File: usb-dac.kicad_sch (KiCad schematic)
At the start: 1 part, among them U1 PCM2706CPJTR

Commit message: Update schematic
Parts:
- removed U1: PCM2706CPJTR, PJT32, symbol 2024-07-12_02-06-17:PCM2706CPJTR
- added P1: USB_C_Plug_USB2.0, symbol Connector:USB_C_Plug_USB2.0
- added U1: PCM2912APJTR, PJT32, symbol 2024-07-12_22-03-46:PCM2912APJTR
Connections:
- new net: P1.A4 (VBUS), P1.A9 (VBUS), P1.B4 (VBUS), P1.B9 (VBUS)
- new net GND: P1.A1 (GND), P1.A12 (GND), P1.B1 (GND), P1.B12 (GND), P1.S1 (SHIELD)
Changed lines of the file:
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@@
 	(paper "A4")
 	(symbol
-		(lib_id "2024-07-12_02-06-17:PCM2706CPJTR")
-		(at 106.68 81.28 0)
+		(lib_id "Connector:USB_C_Plug_USB2.0")
+		(at 67.31 101.6 0)
+		(unit 1)
+		(exclude_from_sim no)
+		(in_bom yes)
+		(on_board yes)
+		(dnp no)
+		(fields_autoplaced yes)
+		(property "Reference" "P1"
+			(at 67.31 78.74 0)
+			(effects
+				(font
+					(size 1.27 1.27)
+				)
+			)
+		)
+		(property "Value" "USB_C_Plug_USB2.0"
+			(at 67.31 81.28 0)
+			(effects
+				(font
+					(size 1.27 1.27)
+				)
+			)
+		)
+		(property "Footprint" ""
+			(at 71.12 101.6 0)
+			(effects
+				(font
+					(size 1.27 1.27)
+				)
+				(hide yes)
+			)
+		)
+		(property "Datasheet" "https://www.usb.org/sites/default/files/documents/usb_type-c.zip"
+			(at 71.12 101.6 0)
+			(effects
+				(font
+					(size 1.27 1.27)
+				)
+				(hide yes)
+			)
+		)
+		(property "Description" "USB 2.0-only Type-C Plug connector"
+			(at 67.31 101.6 0)
+			(effects
+				(font
+					(size 1.27 1.27)
+				)
+				(hide yes)
+			)
+		)
+		(pin "B9"
+		)
+		(pin "S1"
+		)
+		(pin "B12"
+		)
+		(pin "B5"
+		)
+		(pin "B1"
+		)
+		(pin "A5"
+		)
+		(pin "A7"
+		)
+		(pin "A4"
+		)
+		(pin "A1"
+		)
+		(pin "B4"
+		)
+		(pin "A9"
+		)
+		(pin "A12"
+		)
+		(pin "A6"
+		)
+		(instances
+			(project ""
+				(path "/4a7efef3-c114-4eaa-9004-9ebc24c78436"
+					(reference "P1")
+					(unit 1)
+				)
+			)
+		)
+	)
+	(symbol
+		(lib_id "power:GND")
+		(at 67.31 124.46 0)
+		(unit 1)
+		(exclude_from_sim no)
+		(in_bom yes)
+		(on_board yes)
+		(dnp no)
+		(fields_autoplaced yes)
+		(property "Reference" "#PWR01"
+			(at 67.31 130.81 0)
+			(effects
+				(font
+					(size 1.27 1.27)
+				)
+				(hide yes)
+			)
+		)
+		(property "Value" "GND"
+			(at 67.31 129.54 0)
+			(effects
+				(font
+					(size 1.27 1.27)
+				)
+			)
+		)
+		(property "Footprint" ""
+			(at 67.31 124.46 0)
+			(effects
+				(font
+					(size 1.27 1.27)
+				)
+				(hide yes)
+			)
+		)
+		(property "Datasheet" ""
+			(at 67.31 124.46 0)
+			(effects
+				(font
+					(size 1.27 1.27)
+				)
+				(hide yes)
+			)
+		)
+		(property "Description" "Power symbol creates a global label with name \"GND\" , ground"
+			(at 67.31 124.46 0)
+			(effects
+				(font
+					(size 1.27 1.27)
+				)
+				(hide yes)
+			)
+		)
+		(pin "1"
+		)
+		(instances
+			(project ""
+				(path "/4a7efef3-c114-4eaa-9004-9ebc24c78436"
+					(reference "#PWR01")
+					(unit 1)
+				)
+			)
+		)
+	)
+	(symbol
+		(lib_id "power:GND")
+		(at 59.69 124.46 0)
+		(unit 1)
+		(exclude_from_sim no)
+		(in_bom yes)
+		(on_board yes)
+		(dnp no)
+		(fields_autoplaced yes)
+		(property "Reference" "#PWR02"
+			(at 59.69 130.81 0)
+			(effects
+				(font
+					(size 1.27 1.27)
+				)
+				(hide yes)
+			)
+		)
+		(property "Value" "GND"
+			(at 59.69 129.54 0)
+			(effects
+				(font
+					(size 1.27 1.27)
+				)
+			)
+		)
+		(property "Footprint" ""
+			(at 59.69 124.46 0)
+			(effects
+				(font
+					(size 1.27 1.27)
+				)
+				(hide yes)
+			)
+		)
+		(property "Datasheet" ""
+			(at 59.69 124.46 0)
+			(effects
+				(font
+					(size 1.27 1.27)
+				)
+				(hide yes)
+			)
+		)
+		(property "Description" "Power symbol creates a global label with name \"GND\" , ground"
+			(at 59.69 124.46 0)
+			(effects
+				(font
+					(size 1.27 1.27)
+				)
+				(hide yes)
+			)
+		)
+		(pin "1"
+		)
+		(instances
+			(project ""
+				(path "/4a7efef3-c114-4eaa-9004-9ebc24c78436"
+					(reference "#PWR02")
+					(unit 1)
+				)
+			)
+		)
+	)
+	(symbol
+		(lib_id "2024-07-12_22-03-46:PCM2912APJTR")
+		(at 109.22 83.82 0)
 		(unit 1)
 		(exclude_from_sim no)
@@
 		(fields_autoplaced yes)
 		(property "Reference" "U1"
-			(at 142.24 71.12 0)
+			(at 142.24 73.66 0)
 			(effects
 				(font
@@
 			)
 		)
-		(property "Value" "PCM2706CPJTR"
-			(at 142.24 73.66 0)
+		(property "Value" "PCM2912APJTR"
+			(at 142.24 76.2 0)
 			(effects
 				(font
@@
 		)
 		(property "Footprint" "PJT32"
-			(at 140.462 97.282 0)
+			(at 109.22 83.82 0)
 			(effects
 				(font
@@
 			)
 		)
-		(property "Datasheet" "PCM2706CPJTR"
-			(at 140.462 100.33 0)
+		(property "Datasheet" "PCM2912APJTR"
+			(at 109.22 83.82 0)
 			(effects
 				(font
@@
 		)
 		(property "Description" ""
-			(at 106.68 81.28 0)
-			(effects
-				(font
-					(size 1.27 1.27)
-				)
-				(hide yes)
-			)
+			(at 109.22 83.82 0)
+			(effects
+				(font
+					(size 1.27 1.27)
+				)
+				(hide yes)
+			)
+		)
+		(pin "20"
+		)
+		(pin "21"
+		)
+		(pin "22"
+		)
+		(pin "25"
+		)
+		(pin "5"
+		)
+		(pin "19"
+		)
+		(pin "17"
+		)
+		(pin "15"
+		)
+		(pin "26"
+		)
+		(pin "28"
+		)
+		(pin "9"
+		)
+		(pin "27"
+		)
+		(pin "8"
+		)
+		(pin "2"
+		)
+		(pin "18"
+		)
+		(pin "6"
+		)
+		(pin "3"
+		)
+		(pin "29"
+		)
+		(pin "23"
+		)
+		(pin "24"
+		)
+		(pin "7"
+		)
+		(pin "30"
+		)
+		(pin "14"
+		)
+		(pin "12"
+		)
+		(pin "11"
+		)
+		(pin "10"
+		)
+		(pin "1"
+		)
+		(pin "16"
+		)
+		(pin "31"
+		)
+		(pin "13"
+		)
+		(pin "32"
 		)
 		(pin "4"
-		)
-		(pin "6"
-		)
-		(pin "20"
-		)
-		(pin "13"
-		)
-		(pin "2"
-		)
-		(pin "31"
-		)
-		(pin "19"
-		)
-		(pin "32"
-		)
-		(pin "7"
-		)
-		(pin "5"
-		)
-		(pin "25"
-		)
-		(pin "3"
-		)
-		(pin "26"
-		)
-		(pin "24"
-		)
-		(pin "12"
-		)
-		(pin "17"
-		)
-		(pin "15"
-		)
-		(pin "9"
-		)
-		(pin "18"
-		)
-		(pin "21"
-		)
-		(pin "10"
-		)
-		(pin "16"
-		)
-		(pin "14"
-		)
-		(pin "23"
-		)
-		(pin "30"
-		)
-		(pin "8"
-		)
-		(pin "1"
-		)
-		(pin "22"
-		)
-		(pin "27"
-		)
-		(pin "28"
-		)
-		(pin "11"
-		)
-		(pin "29"
 		)
 		(instances
 			(project ""
-				(path "/bb9de763-1d1e-4df2-8e54-dd29f7969205"
+				(path "/4a7efef3-c114-4eaa-9004-9ebc24c78436"
 					(reference "U1")
 					(unit 1)

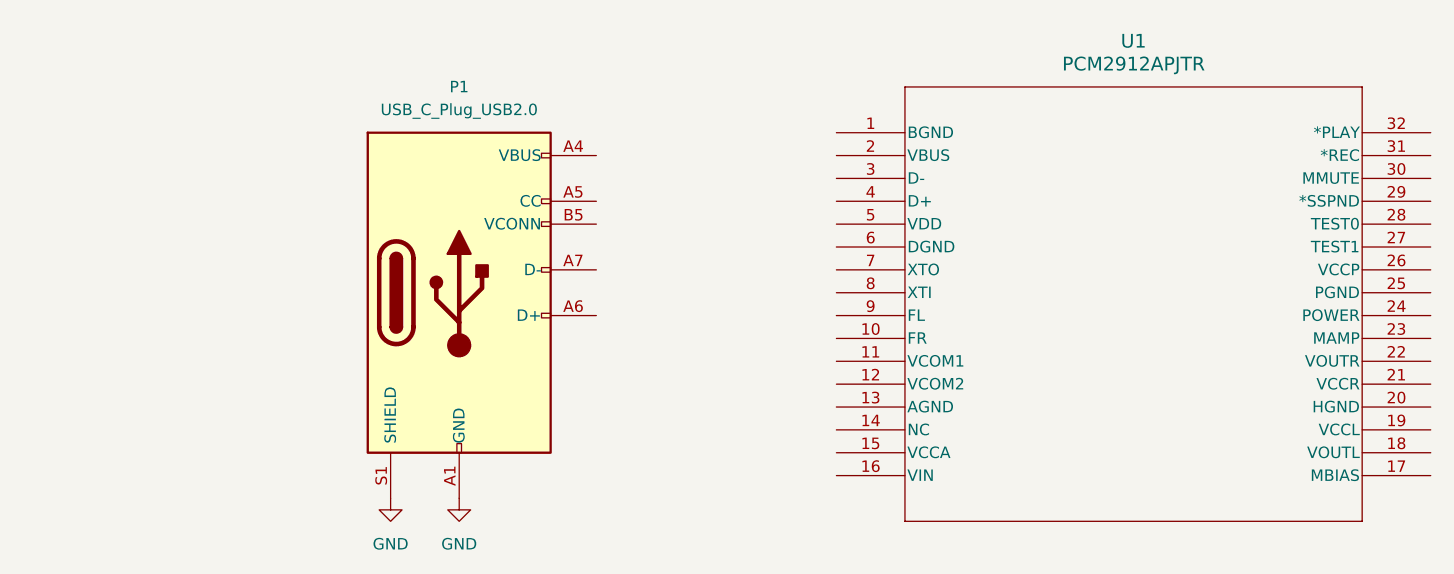
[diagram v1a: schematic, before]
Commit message: update schematic with new components
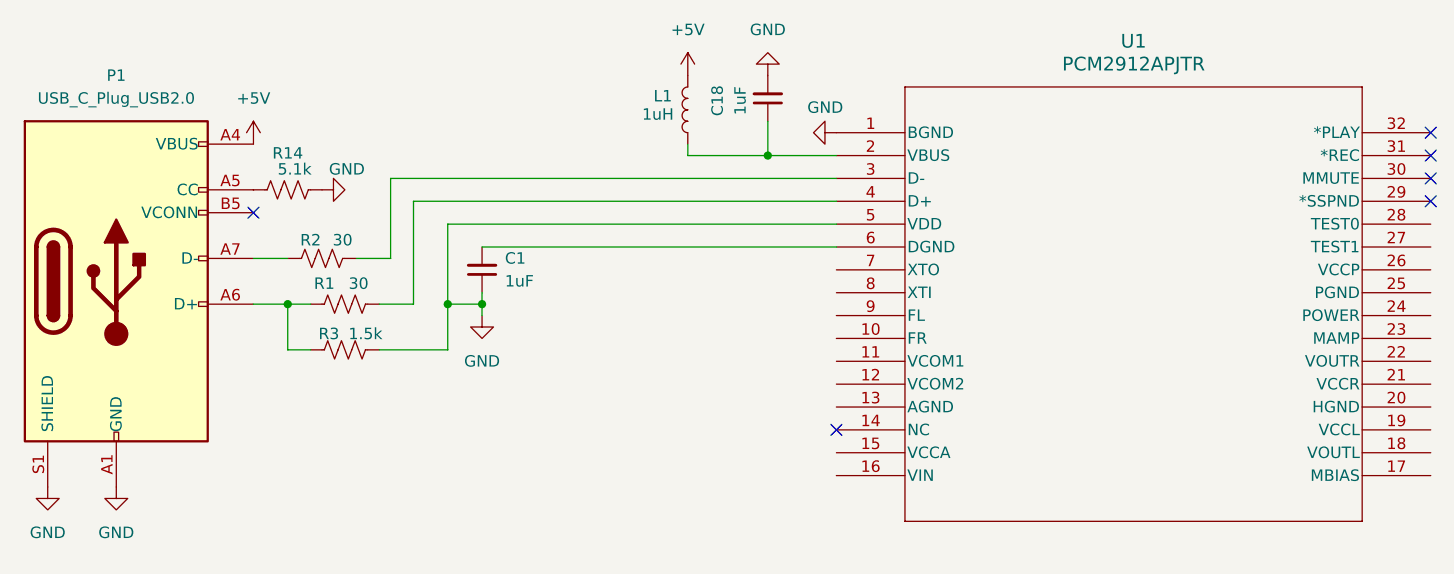
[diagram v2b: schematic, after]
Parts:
- added C1, C18: 1uF, symbol Device:C_Small
- added L1: 1uH, symbol Device:L
- added R1, R2: 30, symbol Device:R_US
- added R14: 5.1k, symbol Device:R_US
- added R3: 1.5k, symbol Device:R_US
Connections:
- net GND: now also U1.1 (BGND), U1.5 (VDD), C1.1, C18.2, R14.1, R3.2
- net +5V: now reaches P1.A4 (VBUS), P1.A9 (VBUS), P1.B4 (VBUS), P1.B9 (VBUS)
- net +5V: now also L1.2
- net at P1.A5 (CC): now also R14.2
- net at P1.A6 (D+): now also R1.1, R3.1
- net at P1.A7 (D-): now also R2.1
- net at U1.2 (VBUS): now also C18.1, L1.1
- net at U1.3 (D-): now also R2.2
- net at U1.4 (D+): now also R1.2
- net at U1.6 (DGND): now also C1.2
- no-connect marks 0 -> 6
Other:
- moved on the sheet: P1

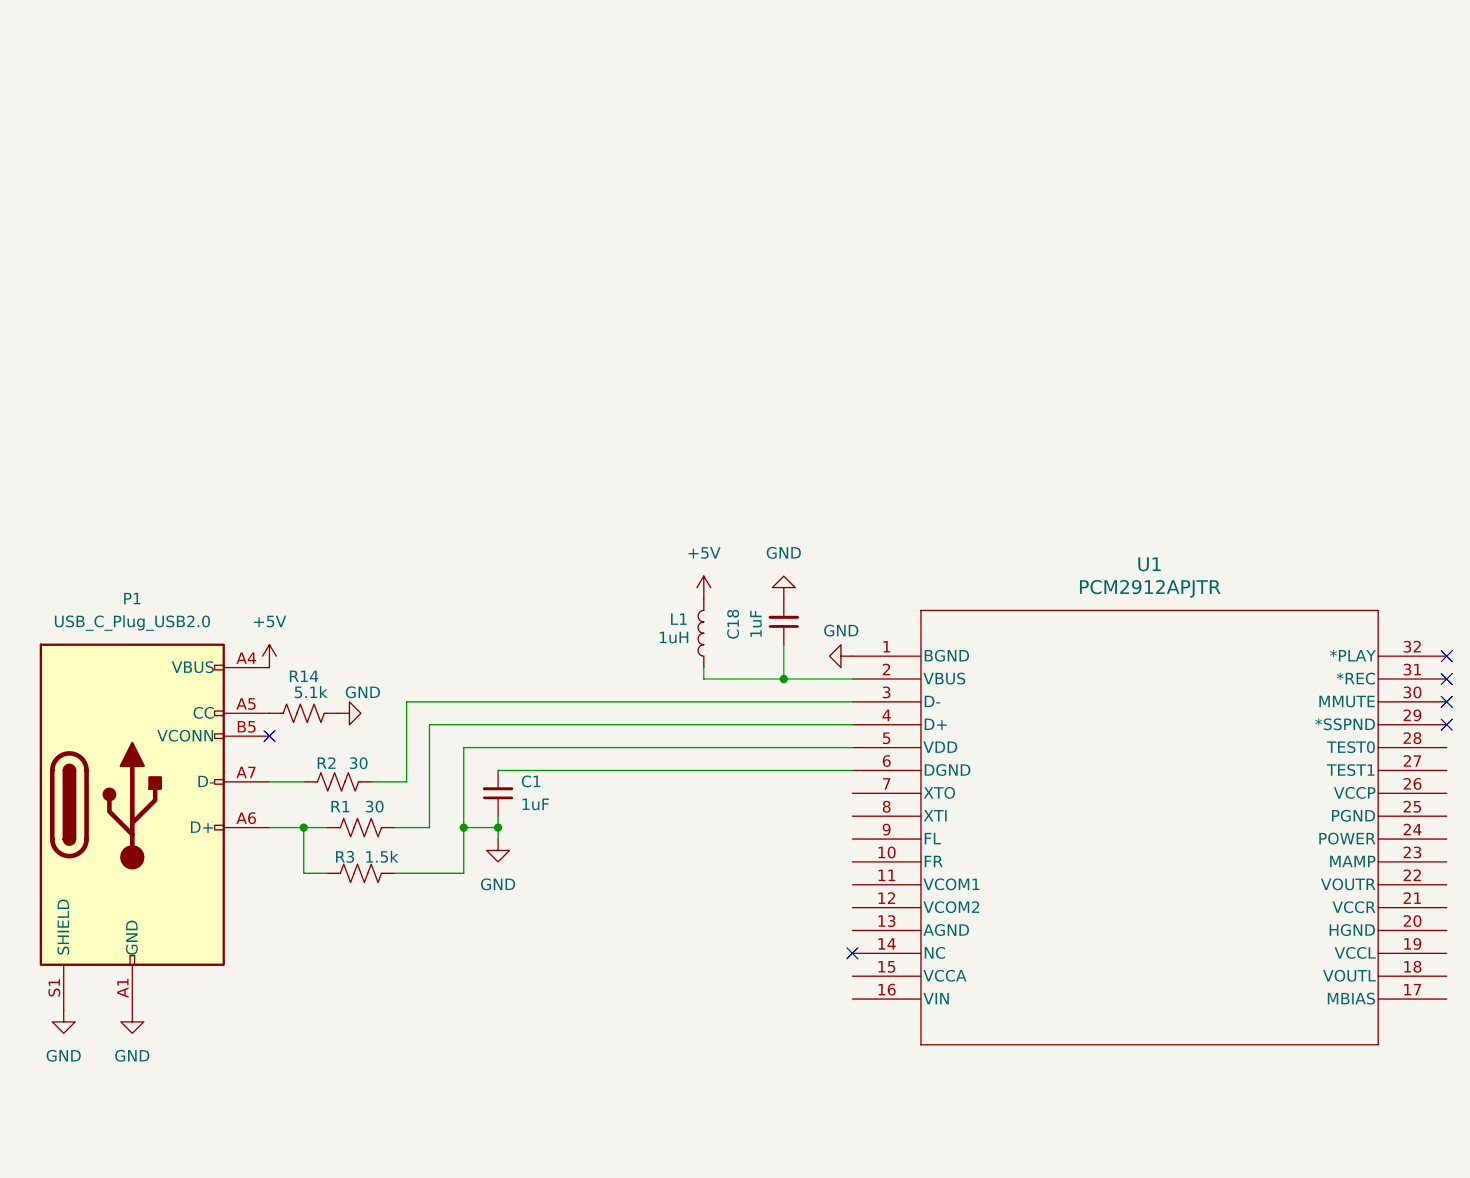
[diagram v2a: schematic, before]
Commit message: Update schematic with separate chunks for different objects
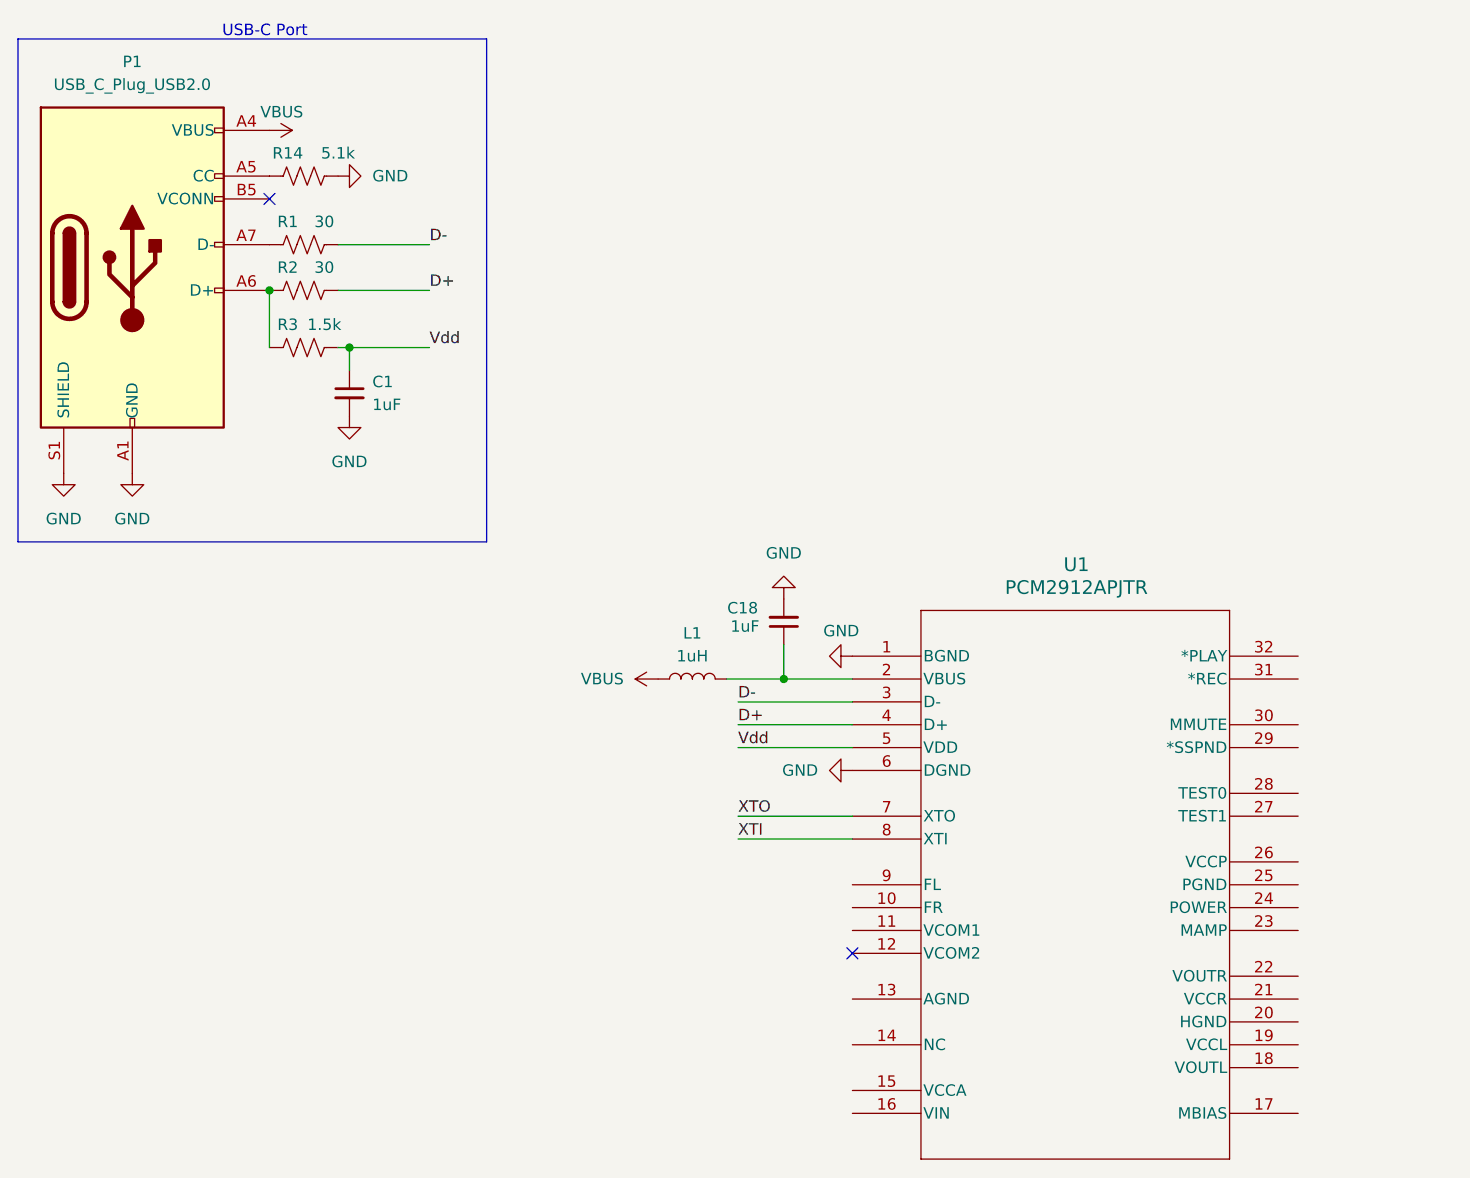
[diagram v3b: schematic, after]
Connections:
- net GND: now also C1.2, R14.2, U1.6 (DGND); no longer C1.1, R14.1, R3.2, U1.5 (VDD)
- net at P1.A6 (D+), R3.1: now also R2.1; no longer R1.1
- net at P1.A5 (CC): now also R14.1; no longer R14.2
- net at P1.A7 (D-): now also R1.1; no longer R2.1
- net D+: now reaches R2.2
- net D+: now also U1.4 (D+); no longer U1.3 (D-)
- net at C18.1, U1.2 (VBUS): now also L1.2; no longer L1.1
- net D-: now reaches R1.2
- net D-: now also U1.3 (D-); no longer U1.4 (D+)
- net XTO: now reaches U1.7 (XTO)
- net XTI: now reaches U1.8 (XTI)
- net +5V renamed VBUS
- net VBUS: now also L1.1; no longer L1.2
- new net Vdd: C1.1, R3.2, U1.5 (VDD)
- no-connect marks 6 -> 2
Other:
- note added: "USB-C Port"
- moved on the sheet: P1, U1

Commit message: Work on schematic
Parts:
- added C2, C3: C_Small, symbol Device:C_Small
- added C4, C5: 100pF, symbol Device:C_Small
- added C6: 3.3uF, symbol Device:C_Small
- added C7: 0.1uF, symbol Device:C_Small
- added R4: 1M, symbol Device:R_US
- added Y1: 6 Mhz, symbol Device:Crystal
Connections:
- net GND: now also U1.13 (AGND), U1.28 (TEST0), C2.2, C3.2, C4.2, C5.2, C6.2, C7.2
- net XTI: now also C3.1, R4.2, Y1.1
- net XTO: now also C2.1, R4.1, Y1.2
- net FR: now reaches U1.10 (FR)
- net FR: now also C5.1
- net VCOM1: now reaches U1.11 (VCOM1)
- net VCOM1: now also C6.1
- net VCOM2: now reaches U1.12 (VCOM2)
- net VCOM2: now also C7.1
- net VCCA: now reaches U1.15 (VCCA)
- net VIN: now reaches U1.16 (VIN)
- net FL: now reaches U1.9 (FL)
- net FL: now also C4.1
- no-connect marks 2 -> 6
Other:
- note added: "Crystal circuit"
- note added: "Decoupling capacitors"
- note added: "Filter capacitors"

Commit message: Some more work on the schematic
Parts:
- added C8: 1uF, symbol Device:C_Small
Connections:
- net VIN is gone; now on net GND: U1.16 (VIN)
- net GND: now also C8.2
- net VCCA: now also C8.1
- net VOUTL: now reaches U1.18 (VOUTL)
- net VCCL: now reaches U1.19 (VCCL)
- net HGND: now reaches U1.20 (HGND)
- net VCCR: now reaches U1.21 (VCCR)
- net VOUTR: now reaches U1.22 (VOUTR)
- no-connect marks 6 -> 7
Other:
- title: (none) -> USB DAC
- moved on the sheet: C18, L1, U1
